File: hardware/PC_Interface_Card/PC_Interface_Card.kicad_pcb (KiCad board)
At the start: 2 copper layers, 146.3 x 70.7 mm, 83 parts, among them J1 GSB1C41110SSHR, J2 DM3BT-DSF-PEJS, J4 BM11B-GHS-TBT, SW1 CherryMX, SW2 CherryMX, SW3 CherryMX, SW4 CherryMX, SW5 CherryMX, SW6 TL1240YQ2JBLK, SW7 TL1240YQ2JBLK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

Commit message: layout changes
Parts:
- removed R28, R30: 68R_0.2W_0603, Resistor_SMD:R_0603_1608Metric
- J1: moved to F.Cu
- SW7, SW8: value TL1240YQ2JBLK -> SW_Push; footprint Footprint:TL1240YQ -> Button_Switch_THT:SW_PUSH_6mm
- U4: footprint RF_Module:ESP32-S3-WROOM-1 -> RF_Module:ESP32-S3-WROOM-1U
- moved J1 212.9 mm to (197.2, -43.3)
- moved R6 202.1 mm to (191.0, -42.0), turned to 180 degrees
- moved R7 202.0 mm to (191.0, -45.0), turned to 180 degrees
- moved F1 200.2 mm to (194.2, -34.5)
- moved FL1 198.7 mm to (195.7, -31.2), turned to -90 degrees
- moved CR1 192.4 mm to (192.6, -28.8), turned to 90 degrees
- moved C4 189.7 mm to (196.3, -25.8)
- moved C3 188.2 mm to (196.3, -24.3)
- moved U2 178.0 mm to (192.6, -20.3), turned to 180 degrees
- moved U1 166.6 mm to (187.8, -43.2)
- moved R21 159.3 mm to (167.4, -25.9)
- moved C13 159.3 mm to (171.1, -22.5)
- moved C15 159.3 mm to (171.1, -20.9)
- moved R12 159.3 mm to (179.1, -27.1)
- moved U3 159.3 mm to (173.2, -26.5)
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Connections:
- SW7 pad 1: SW_EN -> SW_BOOT
- SW7 pad 2: SW_EN -> GND
- SW8 pad 1: SW_BOOT -> SW_EN
- SW8 pad 2: SW_BOOT -> GND
- U4 pad 10: SW_LEFT -> D1_SDMMC
- U4 pad 11: SW_DN -> D2_SDMMC
- U4 pad 12: RST_DISP -> FRAM_CS
- U4 pad 22: FRAM_CS -> RST_DISP
- U4 pad 31: CMD_SDMMC -> SW_RIGHT
- U4 pad 32: CLK_SDMMC -> SW_PLAY
- U4 pad 33: D0_SDMMC -> SW_LEFT
- U4 pad 34: D1_SDMMC -> SW_DN
- U4 pad 35: D2_SDMMC -> ENC_SW
- U4 pad 36: SW_PLAY -> ENC_B
- U4 pad 37: SW_RIGHT -> ENC_A
- U4 pad 4: ENC_A -> unconnected-(U4-IO4-Pad4)
- U4 pad 5: ENC_B -> SW_MENU
- U4 pad 6: ENC_SW -> SW_UP
- U4 pad 7: unconnected-(U4-IO7-Pad7) -> CMD_SDMMC
- U4 pad 8: SW_MENU -> CLK_SDMMC
- U4 pad 9: SW_UP -> D0_SDMMC
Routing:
- net 3V3: track 569.2 -> 411.6 mm, vias 17 -> 9
- net SW_LEFT: track 112.0 -> 6.98 mm, vias 3 -> 0
- net SW_MENU: track 102.9 -> 7.63 mm, vias 4 -> 0
- net CLK_SDMMC: track 91.8 -> 0.00 mm, vias 4 -> 0
- net D1_SDMMC: track 94.8 -> 4.30 mm, vias 4 -> 0
- net D0_SDMMC: track 92.8 -> 4.00 mm, vias 2 -> 0
- net SW_DN: track 95.6 -> 7.26 mm, vias 2 -> 0
- net SW_UP: track 88.1 -> 6.91 mm, vias 2 -> 0
- net CMD_SDMMC: track 80.7 -> 4.87 mm, vias 2 -> 0
- net PWM_DISP: track 21.2 -> 95.5 mm, vias 0 -> 2
- net SW_RIGHT: track 74.1 -> 0.00 mm
- net ENC_A: track 79.3 -> 7.01 mm, vias 4 -> 0
- net SW_EN: track 108.4 -> 40.3 mm
- net D2_SDMMC: track 73.5 -> 7.02 mm, vias 2 -> 0
- net ENC_SW: track 67.2 -> 3.62 mm, vias 1 -> 0
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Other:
- board size 146.3 x 70.7 mm -> 99.1 x 72 mm
- board text removed: "Display Connector"
- board text removed: "Encoder"
- board text removed: "FRAM"
- board text removed: "LDO"
- board text removed: "Play Pause"
- board text removed: "SW DOWN"
- board text removed: "SW LEFT"
- board text removed: "SW UP"
- board text removed: "USB C"
- board text removed: "USB Prot"

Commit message: Saving work with smaller board changes
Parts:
- moved H8 135.7 mm to (80.5, 122.0)
- moved H3 135.7 mm to (80.5, 73.0)
- moved H4 135.7 mm to (22.5, 73.0)
- moved H5 135.7 mm to (22.5, 122.0)
- moved C17 119.3 mm to (144.5, 64.8)
- moved C19 119.3 mm to (158.0, 64.7)
- moved R27 119.3 mm to (147.6, 64.8)
- moved R29 119.3 mm to (154.8, 64.6)
- moved SW7 119.3 mm to (151.7, 67.2)
- moved SW8 119.3 mm to (141.5, 67.2)
- moved R8 117.4 mm to (120.3, 94.4)
- moved J4 117.4 mm to (113.2, 92.8)
- moved H2 117.1 mm to (112.2, 128.9)
- moved H1 117.1 mm to (112.6, 63.2)
- moved C1 117.0 mm to (124.4, 80.3)
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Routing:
- net 3V3: track 411.6 -> 5.80 mm, vias 9 -> 0
- net PWM_DISP: track 95.5 -> 0.00 mm, vias 2 -> 0
- net MOSI: track 92.9 -> 0.00 mm, vias 3 -> 0
- net MISO: track 90.4 -> 0.00 mm, vias 4 -> 0
- net SCLK: track 82.7 -> 0.00 mm, vias 5 -> 0
- net DC_DISP: track 78.2 -> 0.00 mm, vias 2 -> 0
- net RST_DISP: track 77.6 -> 0.00 mm, vias 2 -> 0
- net CS_DISP: track 70.5 -> 0.00 mm, vias 2 -> 0
- net SW_BOOT: track 64.9 -> 0.00 mm, vias 1 -> 0
- net D-: track 0.00 -> 52.9 mm
- net D+: track 0.00 -> 52.9 mm
- net FRAM_CS: track 47.6 -> 0.00 mm, vias 2 -> 0
- net SW_EN: track 40.3 -> 0.00 mm, vias 2 -> 0
- net Net-(SW6-+): track 9.17 -> 0.00 mm
- net Net-(LED3-Pad2): track 8.88 -> 0.00 mm
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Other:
- board size 99.1 x 72 mm -> 91.9 x 72 mm

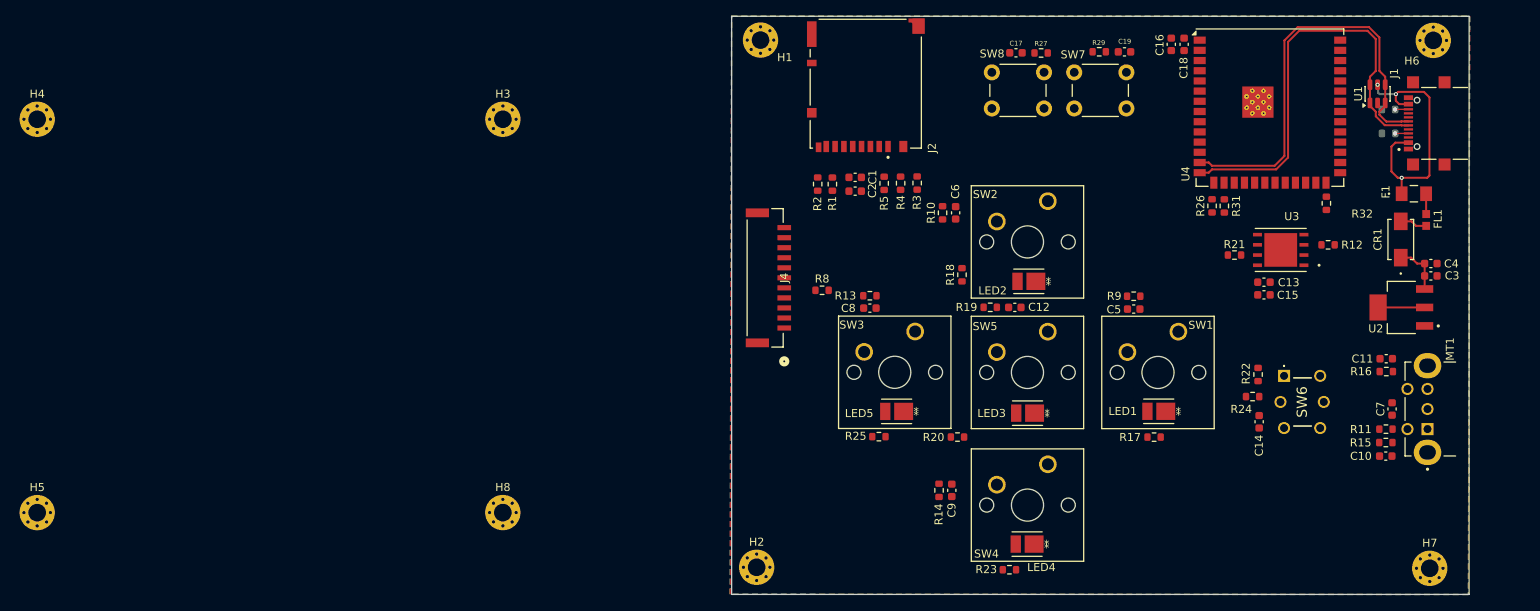
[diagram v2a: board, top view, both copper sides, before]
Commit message: Some DRC errors remain - clarifications on Monday then fab
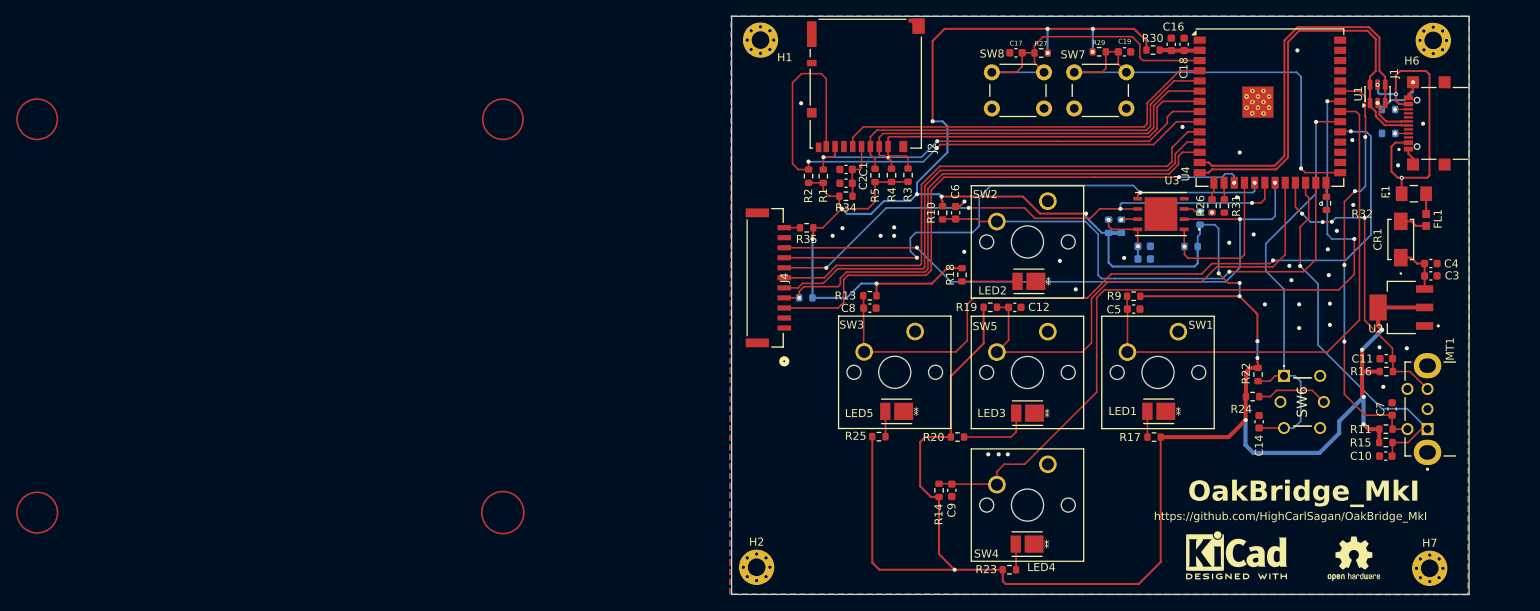
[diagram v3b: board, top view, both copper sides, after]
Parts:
- removed H3, H4, H5, H8: MountingHole_Pad, MountingHole:MountingHole_2.2mm_M2_Pad_Via
- added R28: 10k_0.2W_0603, Resistor_SMD:R_0603_1608Metric, B.Cu at (166.3, 88.9)
- added R30: 0R_0.1W_0603, Resistor_SMD:R_0603_1608Metric, F.Cu at (161.5, 64.4)
- added R33: 0R_0.1W_0603, Resistor_SMD:R_0603_1608Metric, B.Cu at (156.0, 86.4)
- added R34: 0R_0.1W_0603, Resistor_SMD:R_0603_1608Metric, F.Cu at (123.3, 82.6)
- added R35: 0R_0.1W_0603, Resistor_SMD:R_0603_1608Metric, F.Cu at (118.4, 86.6)
- added REF**: KiCad-Logo2_5mm_SilkScreen, Symbol:KiCad-Logo2_5mm_SilkScreen, F.Cu at (171.9, 127.4)
- added REF**: OSHW-Logo2_7.3x6mm_SilkScreen, Symbol:OSHW-Logo2_7.3x6mm_SilkScreen, F.Cu at (186.6, 127.8)
- C13, C15, R12, R21, R8: moved to B.Cu
- moved R12 16.3 mm to (167.4, 85.4), turned to -90 degrees
- moved C13 15.6 mm to (160.4, 88.9)
- moved C15 15.6 mm to (160.4, 90.5)
- moved U3 15.6 mm to (162.5, 84.9)
- moved R21 14.5 mm to (157.6, 86.4), turned to -90 degrees
- moved R8 2.23 mm to (118.3, 95.3)
- moved R5 1.50 mm to (126.9, 80.0)
- moved C1 1.50 mm to (123.3, 79.3)
- moved C2 1.50 mm to (123.3, 81.0)
- moved R1 1.50 mm to (120.5, 80.1)
- moved R2 1.50 mm to (118.6, 80.1)
- moved R3 1.50 mm to (131.0, 80.0)
- moved R4 1.50 mm to (129.0, 80.0)
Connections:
- C1 pad 1: 3V3 -> Net-(J2-VDD)
- C13 pad 1: 3V3 -> Net-(U3-VDD)
- C15 pad 1: 3V3 -> Net-(U3-VDD)
- C16 pad 1: 3V3 -> Net-(U4-3V3)
- C18 pad 1: 3V3 -> Net-(U4-3V3)
- C2 pad 1: 3V3 -> Net-(J2-VDD)
- J2 pad 4: 3V3 -> Net-(J2-VDD)
- J4 pad 11: 3V3 -> Net-(J4-Pin_11)
- R21 pad 1: GND -> Net-(U3-*RESET)
- R21 pad 2: Net-(U3-*RESET) -> 3V3
- U3 pad 8: 3V3 -> Net-(U3-VDD)
- U4 pad 10: D1_SDMMC -> CS_DISP
- U4 pad 11: D2_SDMMC -> DC_DISP
- U4 pad 12: FRAM_CS -> RST_DISP
- U4 pad 17: DC_DISP -> PWM_DISP
- U4 pad 18: CS_DISP -> FRAM_CS
- U4 pad 2: 3V3 -> Net-(U4-3V3)
- U4 pad 22: RST_DISP -> SW_MENU
- U4 pad 23: unconnected-(U4-IO21-Pad23) -> ENC_B
- U4 pad 24: D3_SDMMC -> ENC_A
- U4 pad 25: PWM_DISP -> SW_UP
- U4 pad 36: ENC_B -> unconnected-(U4-RXD0-Pad36)
- U4 pad 37: ENC_A -> unconnected-(U4-TXD0-Pad37)
- U4 pad 4: unconnected-(U4-IO4-Pad4) -> CLK_SDMMC
- U4 pad 5: SW_MENU -> CMD_SDMMC
- U4 pad 6: SW_UP -> D3_SDMMC
- U4 pad 7: CMD_SDMMC -> D2_SDMMC
- U4 pad 8: CLK_SDMMC -> D0_SDMMC
- U4 pad 9: D0_SDMMC -> D1_SDMMC
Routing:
- net 3V3: track 5.80 -> 384.1 mm, vias 0 -> 22
- net SW_DN: track 0.00 -> 96.7 mm, vias 0 -> 2
- net SW_RIGHT: track 0.00 -> 95.2 mm, vias 0 -> 2
- net MISO: track 0.00 -> 81.0 mm, vias 0 -> 3
- net D1_SDMMC: track 0.00 -> 77.6 mm, vias 0 -> 2
- net PWM_DISP: track 0.00 -> 71.5 mm, vias 0 -> 2
- net MOSI: track 0.00 -> 69.5 mm, vias 0 -> 3
- net SCLK: track 0.00 -> 69.0 mm, vias 0 -> 4
- net RST_DISP: track 0.00 -> 66.6 mm, vias 0 -> 1
- net CS_DISP: track 0.00 -> 66.1 mm
- net DC_DISP: track 0.00 -> 65.9 mm
- net SW_LEFT: track 0.00 -> 65.7 mm
- net SW_UP: track 0.00 -> 63.1 mm, vias 0 -> 1
- net SW_MENU: track 0.00 -> 60.8 mm
- net SW_BOOT: track 0.00 -> 55.7 mm, vias 0 -> 1
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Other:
- board text added: "OakBridge_MkI"
- board text added: "https://github.com/HighCarlSagan/OakBridge_MkI"
- board text removed: "EN and BOOT Buttons"
- board text removed: "SDMMC"
- board text removed: "SW MENU"
- board text removed: "SW RIGHT"
